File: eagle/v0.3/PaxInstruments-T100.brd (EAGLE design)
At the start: 46 x 17.1 mm, 32 parts, among them U1 Attiny85

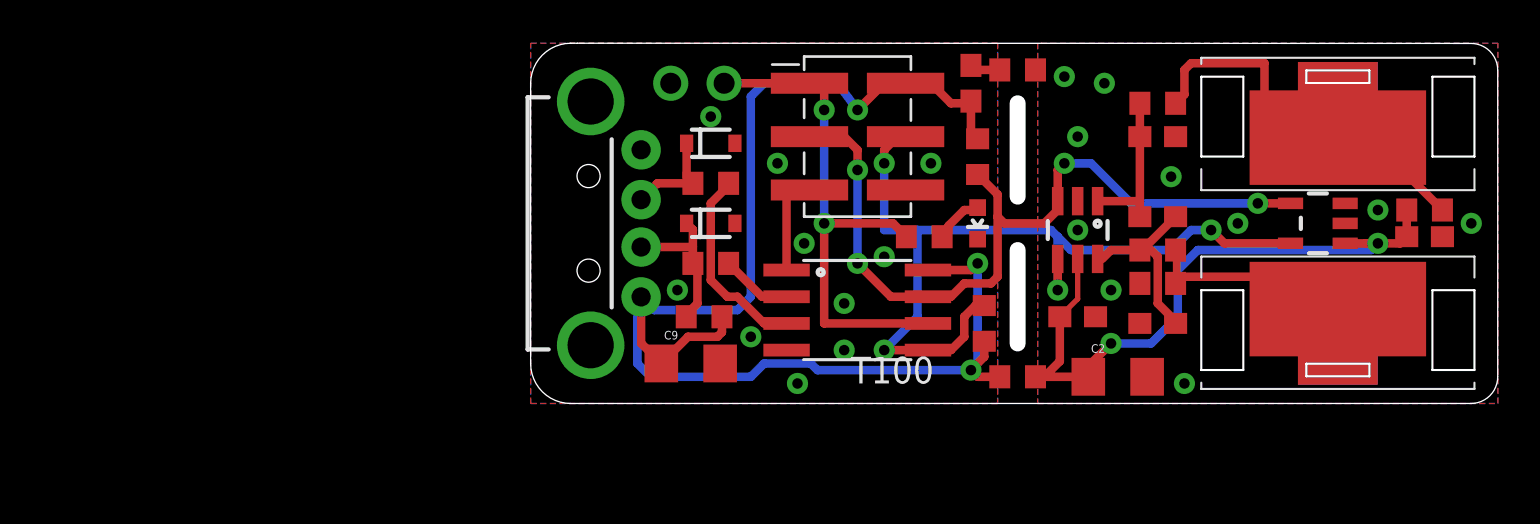
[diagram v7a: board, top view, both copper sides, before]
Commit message: Updated thermocouple connector with th emost recent version.
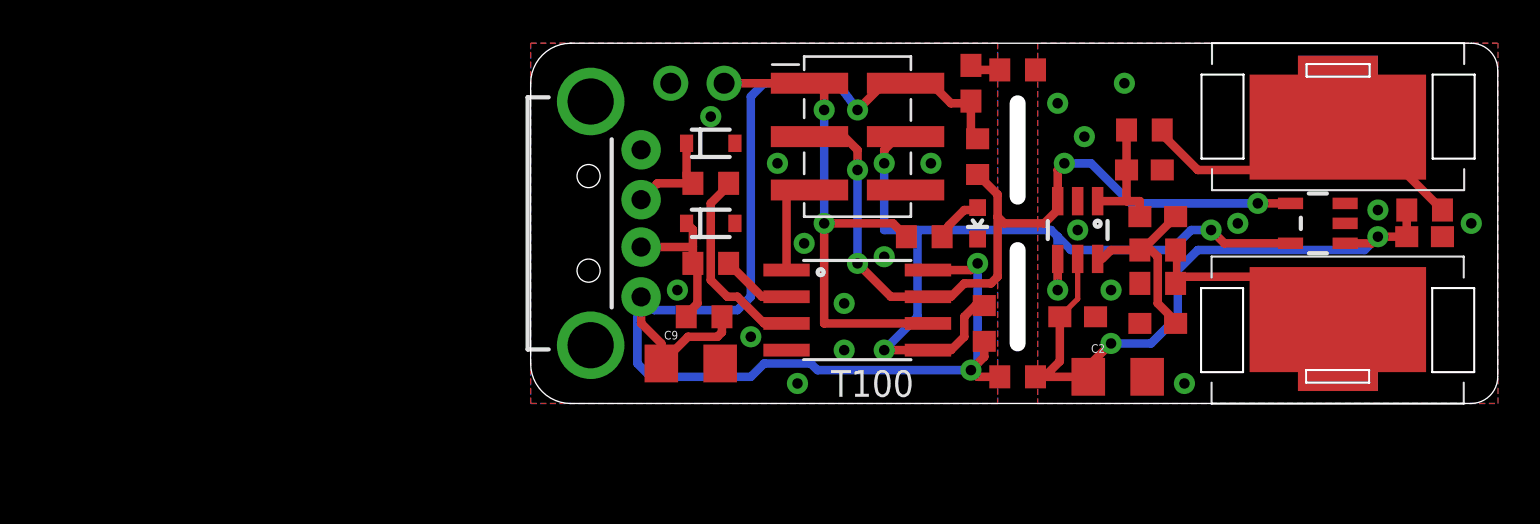
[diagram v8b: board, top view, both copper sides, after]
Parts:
- moved C7 1.71 mm to (29.2, 11.1)
- moved U$1 1.42 mm to (21.9, 10.2)
- moved R6 1.42 mm to (29.2, 13.0)
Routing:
- net N$4: track 19.1 -> 16.6 mm
- net TC+: track 7.41 -> 6.14 mm
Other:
- outline, holes or cut-outs redrawn
- board text added: "TC+"
